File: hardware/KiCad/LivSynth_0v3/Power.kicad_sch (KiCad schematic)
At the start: 61 parts, among them J12 VGND, J201 Test Points, J24 3V3, J25 9V, J7 Barrel_Jack_Switch, Q3 AO3401A, SW7 SW_SPDT, U1 TL074, U12 TPS63070, U2 TL074, U4 TL074, U5 TL074, U6 TL074, U7 LM13700, U8 LM1117-3.3

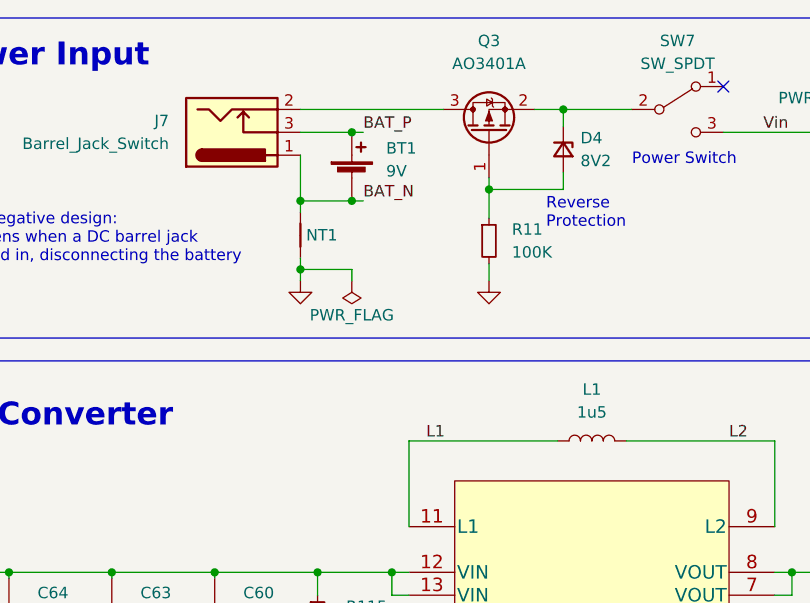
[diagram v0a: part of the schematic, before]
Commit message: Add another LFO cap for easier modding please MCU connectors to the backside Relocate reset button KiCad 7.0.1
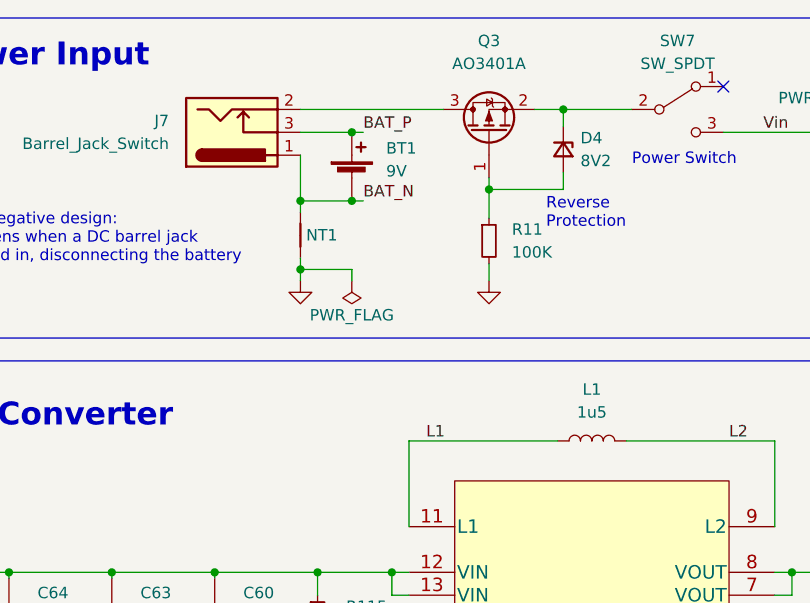
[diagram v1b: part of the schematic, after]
